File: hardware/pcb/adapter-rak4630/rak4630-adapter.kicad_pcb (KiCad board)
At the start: 2 copper layers, 53.6 x 58.4 mm, 26 parts, among them J3 USB-C, J4 SER_SEL, J5 SER_SEL, SW1 RESET, U2 Platform_LoRa, U3 USBLC6-2SC6, U4 RAK4630-8-SM-I, U5 RV-3028-C7

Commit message: Fixed bogus footprints
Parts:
- moved C7 14.6 mm to (160.9, 108.7)
- moved C8 14.6 mm to (160.9, 104.9)
- moved U5 6.31 mm to (160.8, 96.8), turned to 0 degrees
- moved C6 2.30 mm to (160.3, 99.8), turned to 180 degrees
- moved R3 0.79 mm to (164.8, 98.8), turned to -90 degrees
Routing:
- net GND: track 310.5 -> 291.1 mm, vias 44 -> 20
- net Net-(U5-VBACKUP): track 15.9 -> 12.2 mm
- net SDA: track 56.4 -> 59.6 mm
- net SCL: track 53.4 -> 55.6 mm

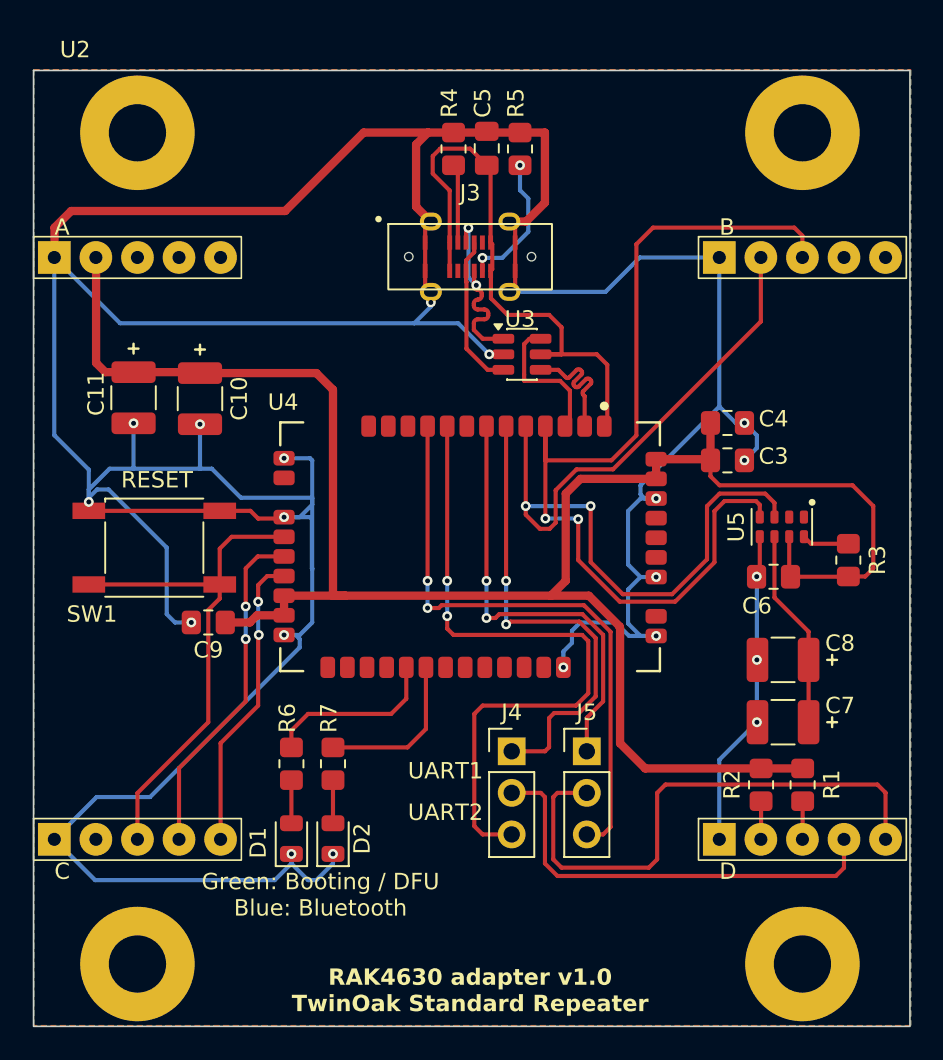
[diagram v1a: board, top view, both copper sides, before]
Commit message: Final PCB adjuments to rev 1.1
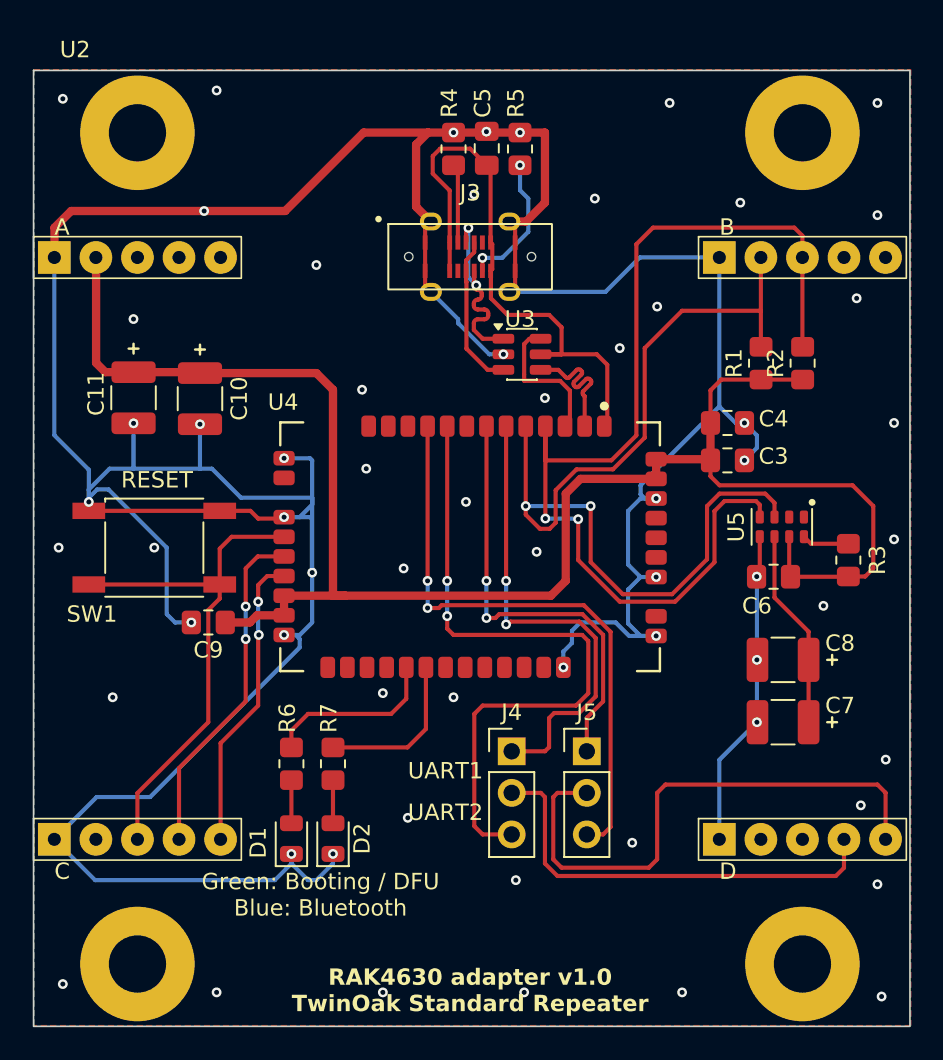
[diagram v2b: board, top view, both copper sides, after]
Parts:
- moved R1 25.9 mm to (159.5, 86.8), turned to 90 degrees
- moved R2 25.9 mm to (162.1, 86.8), turned to 90 degrees
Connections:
- R1 pad 2: Net-(R1-Pad2) -> SCL
- R2 pad 2: Net-(R2-Pad2) -> SDA
- U2 pad 17: Net-(R2-Pad2) -> unconnected-(U2-SCL-Pad17)
- U2 pad 18: Net-(R1-Pad2) -> unconnected-(U2-SDA-Pad18)
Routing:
- net GND: track 291.1 -> 264.1 mm, vias 20 -> 63
- net +3V3: track 122.7 -> 106.7 mm
- net SDA: track 59.6 -> 65.1 mm
- net SCL: track 55.6 -> 60.8 mm
- net Net-(R2-Pad2): track 2.34 -> 0.00 mm
- net Net-(R1-Pad2): track 2.34 -> 0.00 mm

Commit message: Changed via placements to avoid solderwicking
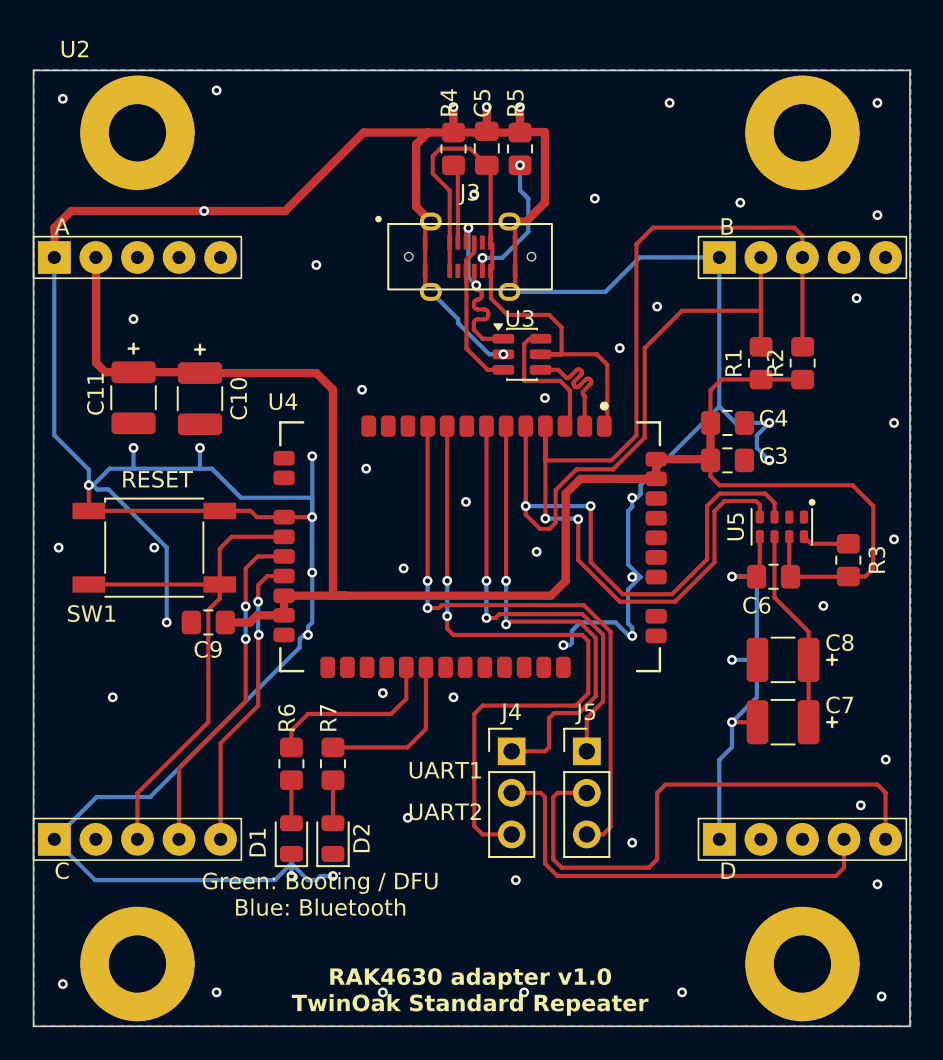
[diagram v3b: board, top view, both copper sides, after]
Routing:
- net GND: track 264.1 -> 259.8 mm

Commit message: Parts ordered!
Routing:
- net Net-(U3-VBUS): track 35.8 -> 46.4 mm, vias 0 -> 2
- net Net-(J3-CC2): track 8.53 -> 9.86 mm
